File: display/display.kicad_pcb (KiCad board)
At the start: 2 copper layers, 177 x 107.2 mm, 19 parts, among them J1 DIN41612_03x32_ABC

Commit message: Ongoing development
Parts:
- moved R12 162.7 mm to (225.5, 114.8), turned to -90 degrees
- moved R11 156.8 mm to (219.8, 114.8), turned to -90 degrees
- moved R9 151.8 mm to (214.1, 114.9), turned to -90 degrees
- moved R10 145.6 mm to (208.4, 114.9), turned to -90 degrees
- moved R6 45.9 mm to (224.8, 74.9), turned to 90 degrees
- moved R2 41.7 mm to (124.6, 62.1)
- moved R1 40.7 mm to (99.7, 62.2)
- moved R4 39.8 mm to (180.2, 62.1)
- moved R3 38.3 mm to (154.2, 62.1)
- moved R8 36.3 mm to (93.7, 114.2), turned to -90 degrees
- moved R5 35.4 mm to (208.6, 62.3)
- moved R7 35.3 mm to (87.1, 114.1), turned to -90 degrees
- moved N6 25.8 mm to (211.0, 82.2)
- moved N5 25.3 mm to (187.0, 82.0)
- moved N1 25.0 mm to (78.1, 81.8)
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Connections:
- J1 pad c11: /T5-9 -> /T5-6
- J1 pad c12: /T5-8 -> /T5-7
- J1 pad c13: /T5-7 -> /T5-8
- J1 pad c14: /T5-6 -> /T5-9
- J1 pad c15: /T5-5 -> /T5-0
- J1 pad c16: /T5-4 -> /T5-1
- J1 pad c17: /T5-3 -> /T5-2
- J1 pad c18: /T5-2 -> /T5-3
- J1 pad c19: /T5-1 -> /T5-4
- J1 pad c20: /T5-0 -> /T5-5
- J1 pad c21: /T4-9 -> /T4-6
- J1 pad c22: /T4-8 -> /T4-7
- J1 pad c23: /T4-7 -> /T4-8
- J1 pad c24: /T4-6 -> /T4-9
- J1 pad c25: /T4-5 -> /T4-0
- J1 pad c26: /T4-4 -> /T4-1
- J1 pad c27: /T4-3 -> /T4-2
- J1 pad c28: /T4-2 -> /T4-3
- J1 pad c29: /T4-1 -> /T4-4
- J1 pad c30: /T4-0 -> /T4-5
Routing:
- net Net-(J1-Pin_b1): track 0.00 -> 357.8 mm, vias 0 -> 6
- net /T5-6: track 0.00 -> 75.5 mm
- net /T5-7: track 0.00 -> 68.7 mm
- net /T6-6: track 0.00 -> 67.0 mm
- net /T6-5: track 0.00 -> 65.9 mm
- net /T6-7: track 0.00 -> 62.6 mm
- net /T4-6: track 0.00 -> 62.4 mm
- net /T5-8: track 0.00 -> 61.9 mm
- net /T6-4: track 0.00 -> 58.9 mm
- net /T5-9: track 0.00 -> 57.6 mm
- net /T6-8: track 0.00 -> 57.1 mm
- net /T4-5: track 0.00 -> 56.9 mm
- net /T4-7: track 0.00 -> 55.5 mm
- net /T6-9: track 0.00 -> 55.0 mm
- net /T6-3: track 0.00 -> 53.1 mm
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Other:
- board size 177 x 107.2 mm -> 165.6 x 69.5 mm

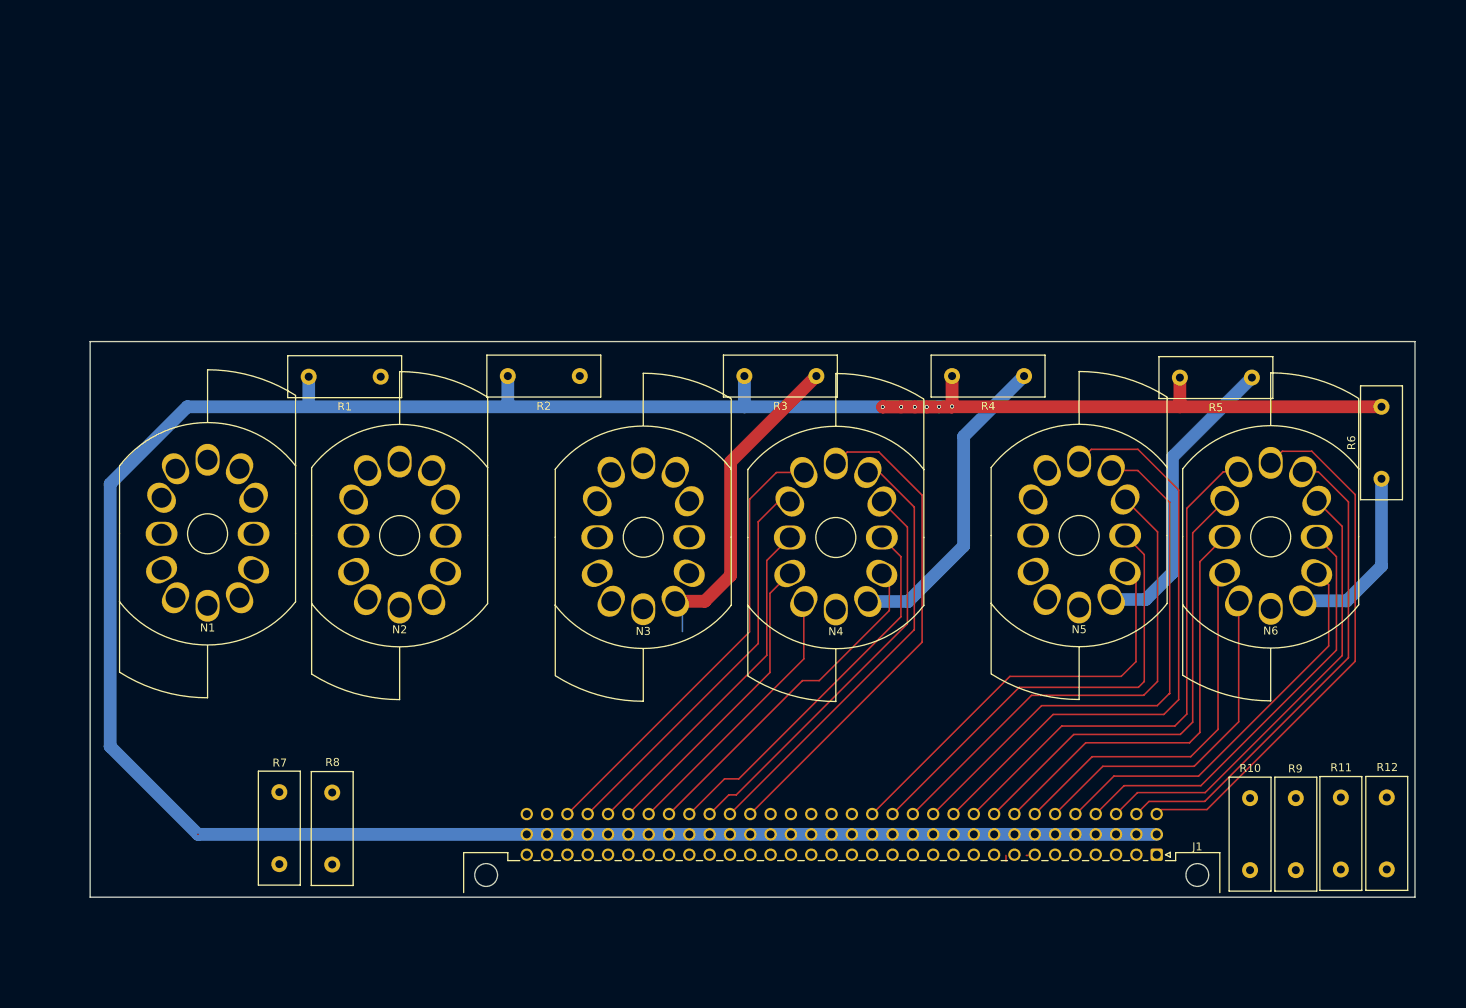
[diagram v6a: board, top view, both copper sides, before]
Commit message: Proposed final display board positioning
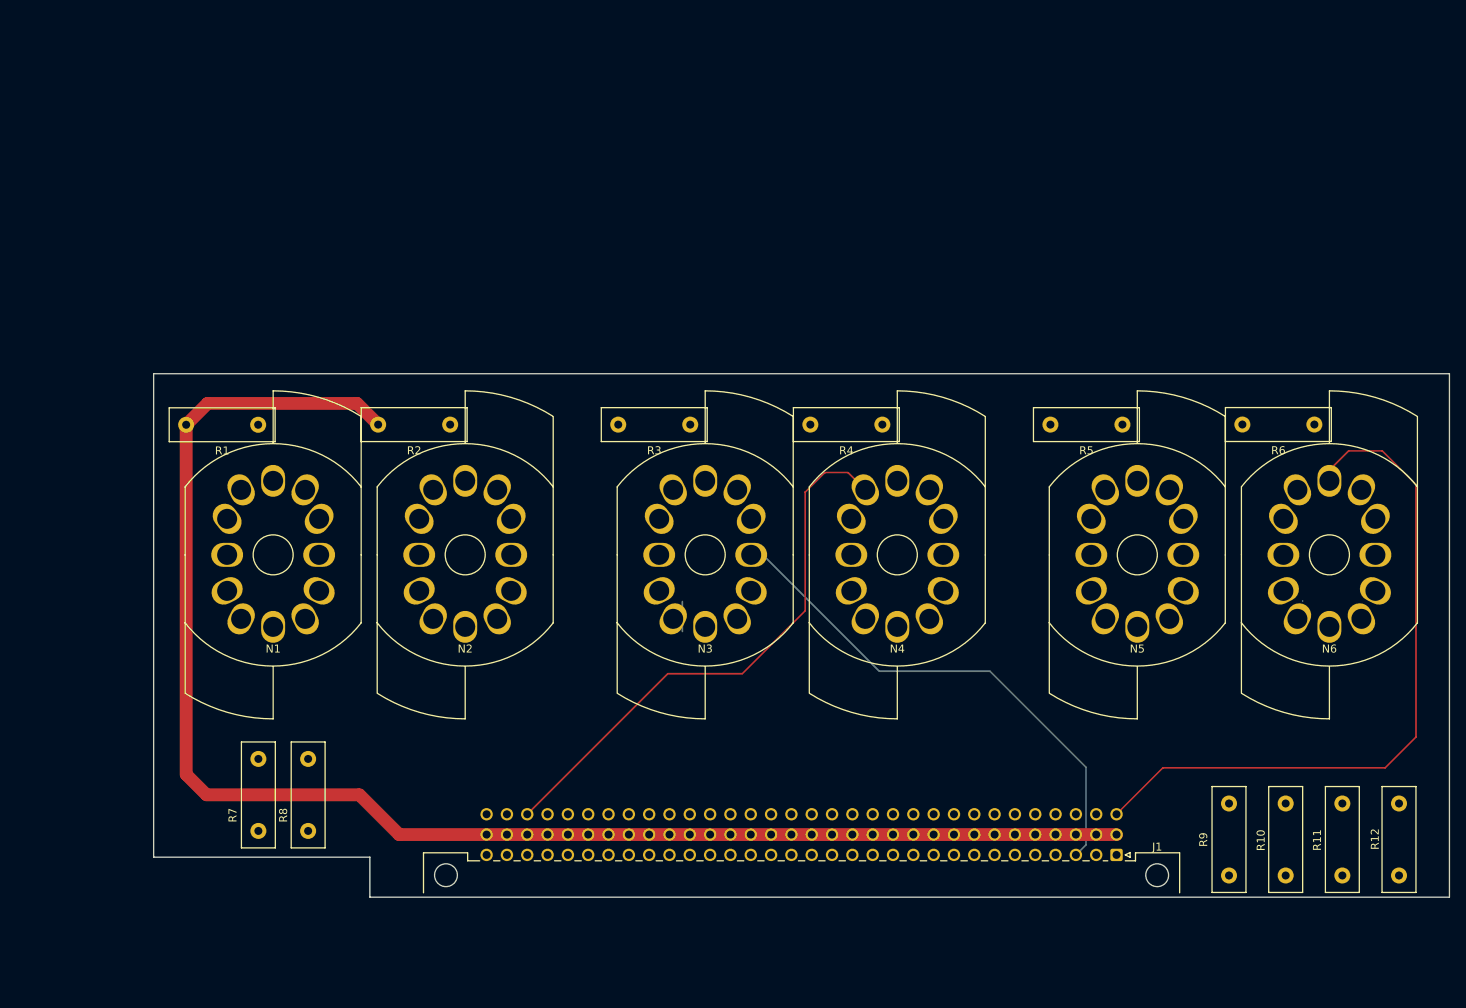
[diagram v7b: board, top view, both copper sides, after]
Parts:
- R1, R10, R11, R12, R2, R3, R4, R5, R6, R7, R8, R9: footprint Resistor_THT:R_Box_L14.0mm_W5.0mm_P9.00mm -> Resistor_THT:R_Box_L13.0mm_W4.0mm_P9.00mm
- moved R4 18.7 mm to (162.4, 68.2)
- moved R2 17.3 mm to (108.4, 68.2)
- moved R5 17.2 mm to (192.5, 68.2)
- moved R3 16.9 mm to (138.4, 68.2)
- moved R1 16.5 mm to (84.4, 68.2)
- moved R6 10.8 mm to (216.4, 68.2), turned to 180 degrees
- moved N1 8.61 mm to (86.3, 84.5)
- moved N2 8.54 mm to (110.3, 84.5)
- moved R9 8.38 mm to (205.8, 115.5)
- moved N3 8.05 mm to (140.3, 84.5)
- moved N4 7.99 mm to (164.3, 84.5)
- moved N6 7.68 mm to (218.3, 84.5)
- moved N5 7.66 mm to (194.3, 84.5)
- moved R8 5.17 mm to (90.7, 110.0)
- moved J1 5.02 mm to (191.7, 122.0)
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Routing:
- net Net-(J1-Pin_b1): track 357.8 -> 189.3 mm, vias 6 -> 0
- net /T5-6: track 75.5 -> 0.00 mm
- net /T5-7: track 68.7 -> 0.00 mm
- net /T6-5: track 65.9 -> 0.00 mm
- net /T3-9: track 0.00 -> 64.3 mm
- net /T6-7: track 62.6 -> 0.00 mm
- net /T4-6: track 62.4 -> 0.00 mm
- net /T5-8: track 61.9 -> 0.00 mm
- net /T6-4: track 58.9 -> 0.00 mm
- net /T5-9: track 57.6 -> 0.00 mm
- net /T6-8: track 57.1 -> 0.00 mm
- net /T4-7: track 55.5 -> 0.00 mm
- net /T6-9: track 55.0 -> 0.00 mm
- net /T6-3: track 53.1 -> 0.00 mm
- net /T5-0: track 52.7 -> 0.00 mm
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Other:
- board size 165.6 x 69.5 mm -> 162 x 65.4 mm

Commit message: Schematic corrected and display board is partially routed
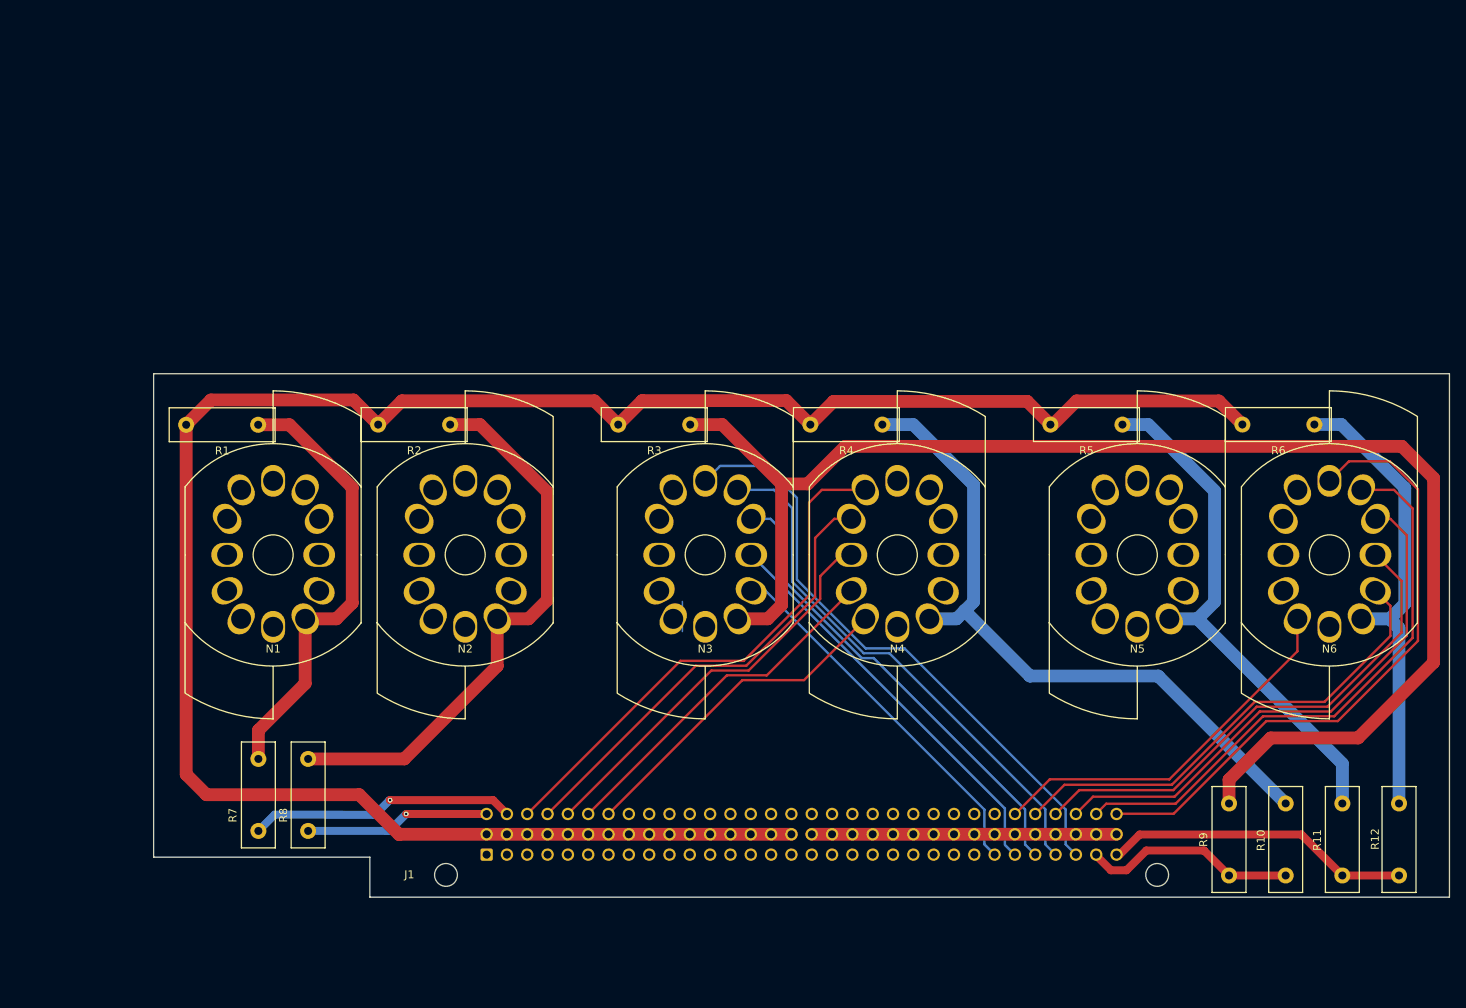
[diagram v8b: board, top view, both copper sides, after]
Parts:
- J1: moved to B.Cu
- moved J1 78.7 mm to (113.0, 121.9), turned to 0 degrees
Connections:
- net Net-(N3-A) renamed MD3
- net Net-(N4-A) renamed MD4
- J1 pad a1: Net-(J1-Pin_a1) -> /T1-5
- J1 pad a10: /T3-2 -> /T1-6
- J1 pad a11: /T3-1 -> /T2-5
- J1 pad a12: /T3-0 -> /T2-4
- J1 pad a13: /T2-9 -> /T2-3
- J1 pad a14: /T2-8 -> /T2-2
- J1 pad a15: /T2-7 -> /T2-1
- J1 pad a16: /T2-6 -> /T2-0
- J1 pad a17: /T2-5 -> /T2-9
- J1 pad a18: /T2-4 -> /T2-8
- J1 pad a19: /T2-3 -> /T2-7
- J1 pad a2: Net-(J1-Pin_a2) -> /T1-4
- J1 pad a20: /T2-2 -> /T2-6
- J1 pad a21: /T2-1 -> /T3-5
- J1 pad a22: /T2-0 -> /T3-4
- J1 pad a23: /T1-9 -> /T3-3
- J1 pad a24: /T1-8 -> /T3-2
- J1 pad a25: /T1-7 -> /T3-1
- J1 pad a26: /T1-6 -> /T3-0
- J1 pad a27: /T1-5 -> /T3-9
- J1 pad a28: /T1-4 -> /T3-8
- J1 pad a29: /T1-3 -> /T3-7
- J1 pad a3: /T3-9 -> /T1-3
- J1 pad a30: /T1-2 -> /T3-6
- J1 pad a31: /T1-1 -> Net-(J1-Pin_a31)
- J1 pad a32: /T1-0 -> Net-(J1-Pin_a32)
- J1 pad a4: /T3-8 -> /T1-2
- J1 pad a5: /T3-7 -> /T1-1
- J1 pad a6: /T3-6 -> /T1-0
- J1 pad a7: /T3-5 -> /T1-9
- J1 pad a8: /T3-4 -> /T1-8
- J1 pad a9: /T3-3 -> /T1-7
- J1 pad b17: Net-(J1-Pin_b1) -> GND
- J1 pad b18: Net-(J1-Pin_b1) -> GND
- J1 pad b19: Net-(J1-Pin_b1) -> GND
- J1 pad b20: Net-(J1-Pin_b1) -> GND
- J1 pad b21: Net-(J1-Pin_b1) -> GND
- J1 pad b22: Net-(J1-Pin_b1) -> GND
- J1 pad b23: Net-(J1-Pin_b1) -> GND
- J1 pad b24: Net-(J1-Pin_b1) -> GND
- J1 pad b25: Net-(J1-Pin_b1) -> GND
- J1 pad b26: Net-(J1-Pin_b1) -> GND
- J1 pad b27: Net-(J1-Pin_b1) -> GND
- J1 pad b28: Net-(J1-Pin_b1) -> GND
- J1 pad b29: Net-(J1-Pin_b1) -> GND
- J1 pad b30: Net-(J1-Pin_b1) -> GND
- J1 pad b31: Net-(J1-Pin_b1) -> GND
- J1 pad b32: Net-(J1-Pin_b1) -> GND
- J1 pad c1: /T6-6 -> Net-(J1-Pin_c1)
- J1 pad c10: /T6-5 -> /T4-8
- J1 pad c11: /T5-6 -> /T4-7
- J1 pad c12: /T5-7 -> /T4-6
- J1 pad c13: /T5-8 -> /T5-5
- J1 pad c14: /T5-9 -> /T5-4
- J1 pad c15: /T5-0 -> /T5-3
- J1 pad c16: /T5-1 -> /T5-2
- J1 pad c17: /T5-2 -> /T5-1
- J1 pad c18: /T5-3 -> /T5-0
- J1 pad c19: /T5-4 -> /T5-9
- J1 pad c2: /T6-7 -> Net-(J1-Pin_c2)
- J1 pad c20: /T5-5 -> /T5-8
- J1 pad c21: /T4-6 -> /T5-7
- J1 pad c22: /T4-7 -> /T5-6
- J1 pad c23: /T4-8 -> /T6-5
- J1 pad c24: /T4-9 -> /T6-4
- J1 pad c25: /T4-0 -> /T6-3
- J1 pad c26: /T4-1 -> /T6-2
- J1 pad c27: /T4-2 -> /T6-1
- J1 pad c28: /T4-3 -> /T6-0
- J1 pad c29: /T4-4 -> /T6-9
- J1 pad c3: /T6-8 -> /T4-5
- J1 pad c30: /T4-5 -> /T6-8
- J1 pad c31: Net-(J1-Pin_c31) -> /T6-7
- J1 pad c32: Net-(J1-Pin_c32) -> /T6-6
- J1 pad c4: /T6-9 -> /T4-4
- J1 pad c5: /T6-0 -> /T4-3
- J1 pad c6: /T6-1 -> /T4-2
- J1 pad c7: /T6-2 -> /T4-1
- J1 pad c8: /T6-3 -> /T4-0
- J1 pad c9: /T6-4 -> /T4-9
- R10 pad 2: Net-(J1-Pin_a2) -> Net-(J1-Pin_a31)
- R11 pad 2: Net-(J1-Pin_a1) -> Net-(J1-Pin_a32)
- R12 pad 2: Net-(J1-Pin_a1) -> Net-(J1-Pin_a32)
- R7 pad 2: Net-(J1-Pin_c31) -> Net-(J1-Pin_c2)
- R8 pad 2: Net-(J1-Pin_c32) -> Net-(J1-Pin_c1)
- R9 pad 2: Net-(J1-Pin_a2) -> Net-(J1-Pin_a31)
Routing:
- net MD3: track 0.00 -> 178.6 mm
- net MD4: track 0.00 -> 85.8 mm
- net Net-(J1-Pin_b1): track 189.3 -> 266.9 mm
- net /T3-6: track 0.00 -> 75.8 mm
- net /T6-7: track 0.00 -> 72.2 mm
- net Net-(N2-A): track 0.00 -> 70.7 mm
- net /T6-8: track 0.00 -> 67.9 mm
- net /T3-7: track 0.00 -> 66.6 mm
- net Net-(N5-A): track 0.00 -> 65.9 mm
- net /T6-9: track 0.00 -> 63.7 mm
- net /T6-0: track 0.00 -> 60.0 mm
- net /T3-8: track 0.00 -> 59.0 mm
- net Net-(N6-A): track 0.02 -> 58.8 mm
- net /T4-4: track 0.00 -> 57.6 mm
- net Net-(N1-A): track 0.00 -> 56.1 mm
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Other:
- copper layers 2 -> 4
